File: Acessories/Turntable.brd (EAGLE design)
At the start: 80 x 50 mm, 31 parts, among them IC1 7812TV, IC2 7805TV, J1 HEADER4, M1 ARDUINO-NANO-3.0, U2 A4988, X1 MKDSN1,5/4-5,08

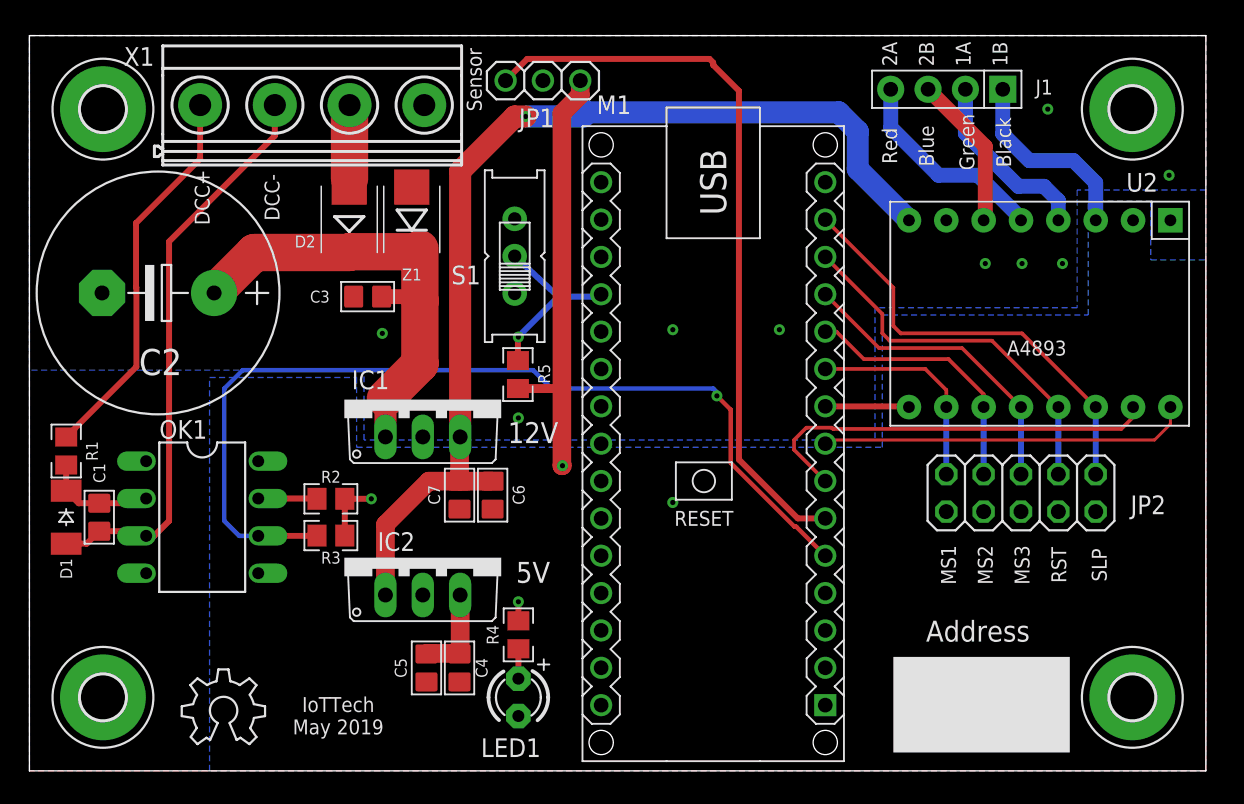
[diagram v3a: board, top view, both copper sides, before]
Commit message: Add files via upload
Updated turntable design, added 3.5mm connector for stepper motor and direct control of the stepping levels
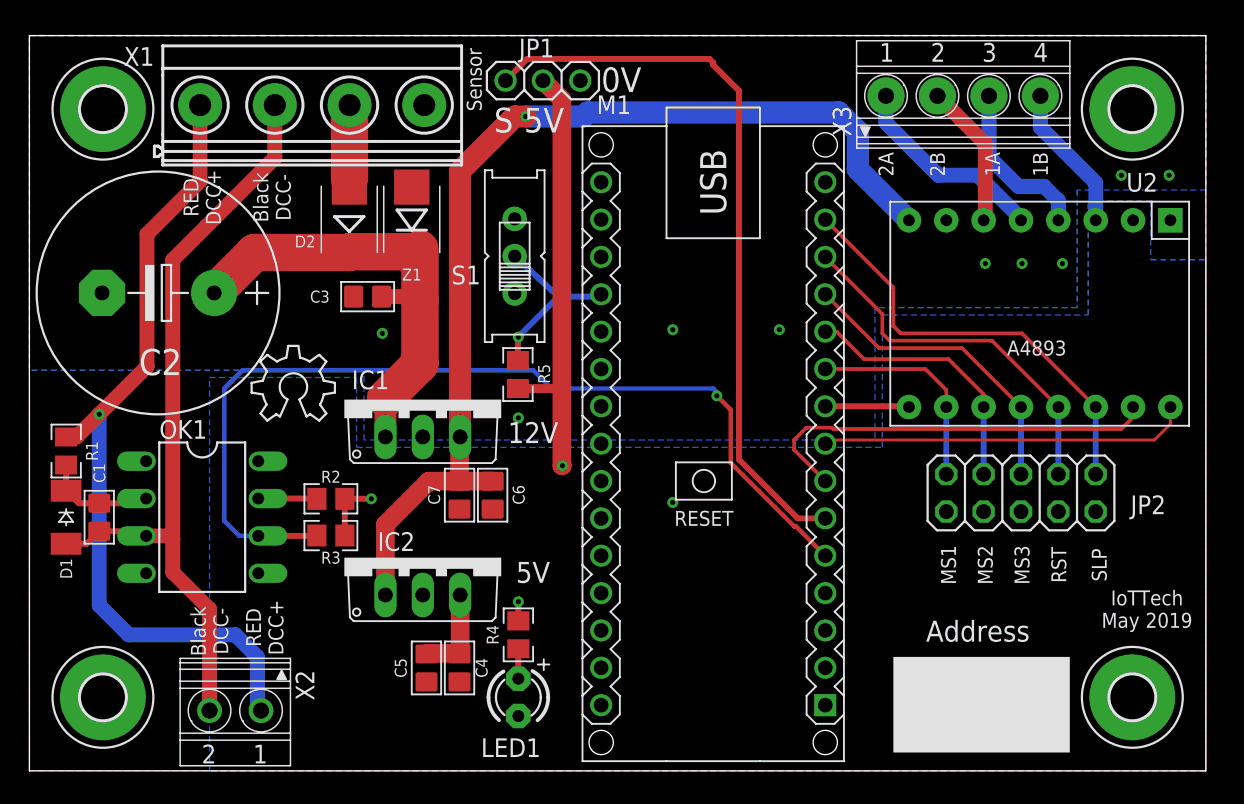
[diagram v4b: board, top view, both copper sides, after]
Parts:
- removed J1: HEADER4, GJR:HEADER4
- added X2: 1751248, con-phoenix-350:1751248
- added X3: 1751264, con-phoenix-350:1751264
- moved LOGO1 22.5 mm to (-24.9, -1.18)
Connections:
- net +5V: now also JP1.2; no longer JP1.3
- net 1A: now also X3.3; no longer J1.2
- net 1B: now also X3.4; no longer J1.1
- net 2A: now also X3.1; no longer J1.4
- net 2B: now also X3.2; no longer J1.3
- net GND: now also JP1.3; no longer JP1.2
- net TRACK1: now also X2.1
- net TRACK2: now also X2.2
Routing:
- net TRACK1: track 26.4 -> 55.7 mm, vias 0 -> 1
- net TRACK2: track 39.1 -> 52.9 mm
- net 1B: track 13.3 -> 10.0 mm
- net 1A: track 12.6 -> 11.4 mm
- net 2B: track 10.6 -> 9.85 mm
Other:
- board text added: "0V"
- board text added: "Black DCC-"
- board text added: "RED DCC+"
- board text added: "S"
- board text removed: "Black"
- board text removed: "Blue"
- board text removed: "DCC+"
- board text removed: "DCC-"
- board text removed: "Green"
- board text removed: "Red"

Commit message: Add files via upload
added 2 more sensor inputs to enable multiple sensing locations. Intended home, first engine, last engine
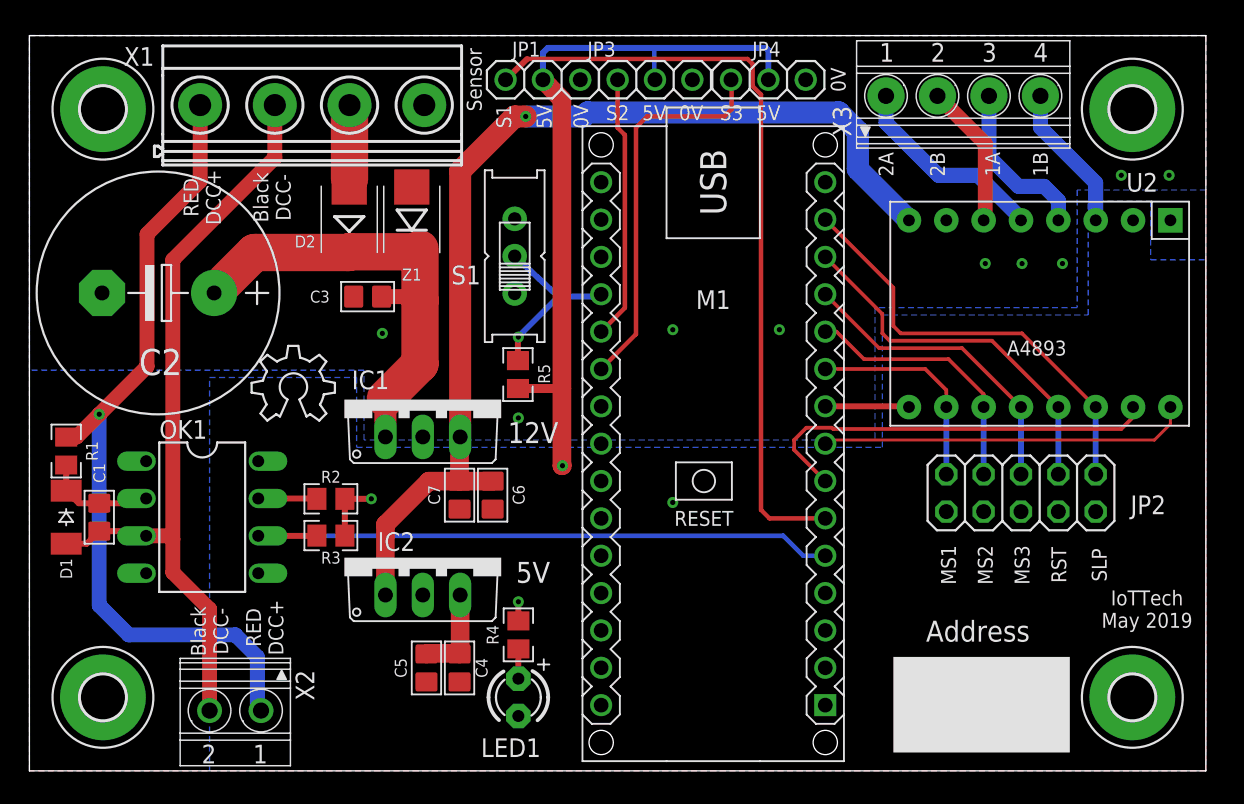
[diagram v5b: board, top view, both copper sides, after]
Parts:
- added JP3, JP4: (no value), adafruit:1X03
- moved JP1 0.06 mm to (-5.08, 22.0)
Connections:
- net POS renamed POS1
- new net POS2: JP3.1, M1.J2.11
- new net POS3: JP4.1, M1.J2.10
- net +5V: now also JP3.2, JP4.2
- net GND: now also JP3.3, JP4.3
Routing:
- net POS3: track 0.00 -> 26.4 mm
- net +5V: track 41.9 -> 63.5 mm
- net DCCIN: track 64.6 -> 43.1 mm, vias 1 -> 0
- net POS2: track 0.00 -> 18.0 mm
- net POS1: track 50.1 -> 52.7 mm
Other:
- board text added: "S1"
- board text added: "S2"
- board text added: "S3"
- board text removed: "S"
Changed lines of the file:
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@@
 <text x="36" y="-14" size="1.016" layer="21" align="center">IoTTech
 May 2019</text>
-<text x="-7.75" y="19.25" size="1.6764" layer="21" align="center">S</text>
-<text x="-5" y="19.25" size="1.6764" layer="21" align="center">5V</text>
-<text x="0.25" y="22" size="1.6764" layer="21" align="center">0V</text>
+<text x="-7.75" y="19.5" size="1.016" layer="21" rot="R90" align="center">S1</text>
+<text x="-5" y="19.5" size="1.016" layer="21" rot="R90" align="center">5V</text>
+<text x="-2.5" y="19.5" size="1.016" layer="21" rot="R90" align="center">0V</text>
 <text x="-24" y="-15.25" size="1.016" layer="21" rot="R90" align="center">RED
 DCC+</text>
 <text x="-27.75" y="-15.5" size="1.016" layer="21" rot="R90" align="center">Black
 DCC-</text>
+<text x="15" y="22" size="1.016" layer="21" rot="R90" align="center">0V</text>
+<text x="5" y="19.75" size="1.016" layer="21" rot="R180" align="center">0V</text>
+<text x="2.5" y="19.75" size="1.016" layer="21" rot="R180" align="center">5V</text>
+<text x="10.25" y="19.75" size="1.016" layer="21" rot="R180" align="center">5V</text>
+<text x="0" y="19.75" size="1.016" layer="21" rot="R180" align="center">S2</text>
+<text x="7.75" y="19.75" size="1.016" layer="21" rot="R180" align="center">S3</text>
 </plain>
 <attributes>
@@
 </element>
 <element name="M1" library="diy-modules" package="ARDUINO-NANO-3.0" value="ARDUINO-NANO-3.0" x="6.5" y="-2.75" smashed="yes" rot="R270">
-<attribute name="NAME" x="-0.25" y="19.66" size="1.27" layer="25" align="bottom-center"/>
+<attribute name="NAME" x="6.5" y="6.41" size="1.27" layer="25" align="bottom-center"/>
 <attribute name="VALUE" x="-3.66" y="-2.75" size="1.27" layer="27" rot="R270" align="top-center"/>
 </element>
@@
 <element name="H3" library="holes" package="3,0-PAD" value="MOUNT-PAD-ROUND3.0" x="-35" y="-20" smashed="yes"/>
 <element name="H4" library="holes" package="3,0-PAD" value="MOUNT-PAD-ROUND3.0" x="-35" y="20" smashed="yes"/>
-<element name="JP1" library="adafruit" library_urn="urn:adsk.eagle:library:420" package="1X03" package3d_urn="urn:adsk.eagle:package:6240710/1" value="" x="-5.08" y="21.94" smashed="yes">
-<attribute name="NAME" x="-6.7162" y="23.5188" size="1.27" layer="25" ratio="10"/>
-<attribute name="VALUE" x="-8.89" y="18.765" size="1.27" layer="27"/>
+<element name="JP1" library="adafruit" library_urn="urn:adsk.eagle:library:420" package="1X03" package3d_urn="urn:adsk.eagle:package:6240710/1" value="" x="-5.08" y="22" smashed="yes">
+<attribute name="NAME" x="-6.2162" y="24.0788" size="1.016" layer="25" ratio="10" align="center"/>
+<attribute name="VALUE" x="-8.89" y="18.825" size="1.27" layer="27"/>
 </element>
 <element name="LOGO1" library="ohw-logo" package="OSHW_6X200_NOTEXT" value="OSHW_LOGO_6MILX0200-NT" x="-24.89" y="-1.18" smashed="yes"/>
@@
 <attribute name="OC_NEWARK" value="unknown" x="-26" y="-21" size="1.778" layer="27" rot="R180" display="off"/>
 <attribute name="VALUE" x="-23.9475" y="-25.1275" size="1.27" layer="27" rot="R180"/>
+</element>
+<element name="JP3" library="adafruit" library_urn="urn:adsk.eagle:library:420" package="1X03" package3d_urn="urn:adsk.eagle:package:6240710/1" value="" x="2.54" y="22" smashed="yes">
+<attribute name="NAME" x="-1.0962" y="24.0788" size="1.016" layer="25" ratio="10" align="center"/>
+<attribute name="VALUE" x="-1.27" y="18.825" size="1.27" layer="27"/>
+</element>
+<element name="JP4" library="adafruit" library_urn="urn:adsk.eagle:library:420" package="1X03" package3d_urn="urn:adsk.eagle:package:6240710/1" value="" x="10.25" y="22" smashed="yes">
+<attribute name="NAME" x="10.1138" y="24.0788" size="1.016" layer="25" ratio="10" align="center"/>
+<attribute name="VALUE" x="6.44" y="18.825" size="1.27" layer="27"/>
 </element>
 </elements>
@@
 <contactref element="IC1" pad="2"/>
 <contactref element="IC2" pad="2"/>
+<contactref element="JP3" pad="3"/>
 <contactref element="JP1" pad="3"/>
+<contactref element="JP4" pad="3"/>
 </signal>
 <signal name="+5V">
@@
 <via x="-16.75" y="-6.5" extent="1-16" drill="0.35"/>
 <contactref element="JP1" pad="2"/>
-<wire x1="-5.08" y1="21.94" x2="-3.79" y2="20.65" width="1.27" layer="1"/>
+<wire x1="-5.08" y1="22" x2="-3.79" y2="20.65" width="1.27" layer="1"/>
 <wire x1="-3.79" y1="20.65" x2="-3.79" y2="1" width="1.27" layer="1"/>
+<contactref element="JP3" pad="2"/>
+<contactref element="JP4" pad="2"/>
+<wire x1="-5.08" y1="22" x2="-5.08" y2="23.8318" width="0.4064" layer="16"/>
+<wire x1="-5.08" y1="23.8318" x2="-4.75" y2="24.1618" width="0.4064" layer="16"/>
+<wire x1="-4.75" y1="24.1618" x2="2.5" y2="24.1618" width="0.4064" layer="16"/>
+<wire x1="2.5" y1="24.1618" x2="10.0882" y2="24.1618" width="0.4064" layer="16"/>
+<wire x1="10.0882" y1="24.1618" x2="10.25" y2="24" width="0.4064" layer="16"/>
+<wire x1="10.25" y1="24" x2="10.25" y2="22" width="0.4064" layer="16"/>
+<wire x1="2.5" y1="24.1618" x2="2.5" y2="22.04" width="0.3048" layer="16"/>
+<wire x1="2.5" y1="22.04" x2="2.54" y2="22" width="0.3048" layer="16"/>
 </signal>
 <signal name="DCCIN">
@@
 <contactref element="OK1" pad="6"/>
 <contactref element="M1" pad="J1.5"/>
-<wire x1="-24.44" y1="-9.02" x2="-25.73" y2="-9.02" width="0.3048" layer="16"/>
-<wire x1="-25.73" y1="-9.02" x2="-26.75" y2="-8" width="0.3048" layer="16"/>
-<wire x1="-26.75" y1="-8" x2="-26.75" y2="1" width="0.3048" layer="16"/>
-<wire x1="-26.75" y1="1" x2="-25.5" y2="2.25" width="0.3048" layer="16"/>
-<wire x1="-25.5" y1="2.25" x2="-5.75" y2="2.25" width="0.3048" layer="16"/>
-<wire x1="-5.75" y1="2.25" x2="-4.5" y2="1" width="0.3048" layer="16"/>
-<wire x1="6.5" y1="1" x2="6.75" y2="0.75" width="0.3048" layer="16"/>
-<wire x1="6.75" y1="0.75" x2="6.75" y2="0.5" width="0.3048" layer="16"/>
-<via x="6.75" y="0.5" extent="1-16" drill="0.35"/>
-<wire x1="6.75" y1="0.5" x2="7.6912" y2="-0.4412" width="0.3048" layer="1"/>
-<wire x1="7.6912" y1="-0.4412" x2="7.6912" y2="-4.06146875" width="0.3048" layer="1"/>
-<wire x1="7.6912" y1="-4.06146875" x2="12.01853125" y2="-8.3888" width="0.3048" layer="1"/>
-<wire x1="12.01853125" y1="-8.3888" x2="12.1388" y2="-8.3888" width="0.3048" layer="1"/>
-<wire x1="12.1388" y1="-8.3888" x2="14.12" y2="-10.37" width="0.3048" layer="1"/>
-<wire x1="-4.5" y1="1" x2="6.5" y2="1" width="0.3048" layer="16"/>
+<wire x1="11.25" y1="-9" x2="12.62" y2="-10.37" width="0.3048" layer="16"/>
 <wire x1="-24.44" y1="-9.02" x2="-20.47" y2="-9.02" width="0.4064" layer="1"/>
 <wire x1="-20.47" y1="-9.02" x2="-20.45" y2="-9" width="0.4064" layer="1"/>
+<wire x1="14.12" y1="-10.37" x2="12.62" y2="-10.37" width="0.3048" layer="16"/>
+<wire x1="-24.44" y1="-9.02" x2="11.23" y2="-9.02" width="0.3048" layer="16"/>
+<wire x1="11.23" y1="-9.02" x2="11.25" y2="-9" width="0.3048" layer="16"/>
 </signal>
 <signal name="N$2">
@@
 <wire x1="19.76" y1="-0.21" x2="19.81" y2="-0.26" width="0.4064" layer="1"/>
 </signal>
-<signal name="POS">
+<signal name="POS1">
+<contactref element="JP1" pad="1"/>
+<wire x1="-7.62" y1="22" x2="-6.1482" y2="23.4118" width="0.4064" layer="1"/>
 <contactref element="M1" pad="J1.6"/>
-<contactref element="JP1" pad="1"/>
-<wire x1="14.12" y1="-7.83" x2="12.25" y2="-7.83" width="0.4064" layer="1"/>
-<wire x1="12.25" y1="-7.83" x2="8.25" y2="-3.83" width="0.4064" layer="1"/>
-<wire x1="6.5" y1="23" x2="8.25" y2="21.25" width="0.4064" layer="1"/>
-<wire x1="8.25" y1="-3.83" x2="8.25" y2="21.25" width="0.4064" layer="1"/>
-<wire x1="-7.62" y1="21.94" x2="-6.1482" y2="23.4118" width="0.4064" layer="1"/>
-<wire x1="-6.1482" y1="23.4118" x2="6.25" y2="23.4118" width="0.4064" layer="1"/>
-<wire x1="6.25" y1="23.4118" x2="6.5" y2="23.1618" width="0.4064" layer="1"/>
-<wire x1="6.5" y1="23.1618" x2="6.5" y2="23" width="0.4064" layer="1"/>
+<wire x1="-6.1482" y1="23.4118" x2="8.8382" y2="23.4118" width="0.3048" layer="1"/>
+<wire x1="9.75" y1="20.9913125" x2="9.75" y2="-7.25" width="0.3048" layer="1"/>
+<wire x1="9.1832" y1="23.0668" x2="9.1832" y2="21.5581125" width="0.3048" layer="1"/>
+<wire x1="9.1832" y1="21.5581125" x2="9.75" y2="20.9913125" width="0.3048" layer="1"/>
+<wire x1="9.75" y1="-7.25" x2="10.33" y2="-7.83" width="0.3048" layer="1"/>
+<wire x1="10.33" y1="-7.83" x2="14.12" y2="-7.83" width="0.3048" layer="1"/>
+<wire x1="8.8382" y1="23.4118" x2="9.1832" y2="23.0668" width="0.3048" layer="1"/>
 </signal>
 <signal name="STEP">
@@
 <wire x1="19.25" y1="4.75" x2="27.5" y2="4.75" width="0.254" layer="1"/>
 </signal>
+<signal name="POS2">
+<contactref element="JP3" pad="1"/>
+<contactref element="M1" pad="J2.11"/>
+<wire x1="0.4929" y1="18.2380875" x2="0" y2="18.7309875" width="0.3048" layer="1"/>
+<wire x1="0" y1="18.7309875" x2="0" y2="22" width="0.3048" layer="1"/>
+<wire x1="-1.12" y1="4.87" x2="0.4929" y2="6.4829" width="0.3048" layer="1"/>
+<wire x1="0.4929" y1="6.4829" x2="0.4929" y2="18.2380875" width="0.3048" layer="1"/>
+</signal>
+<signal name="POS3">
+<contactref element="JP4" pad="1"/>
+<contactref element="M1" pad="J2.10"/>
+<wire x1="-1.12" y1="2.33" x2="1.25" y2="4.7" width="0.3048" layer="1"/>
+<wire x1="1.25" y1="18.75" x2="2" y2="19.5" width="0.3048" layer="1"/>
+<wire x1="7.25" y1="19.5" x2="7.75" y2="20" width="0.3048" layer="1"/>
+<wire x1="7.75" y1="20" x2="7.75" y2="21.96" width="0.3048" layer="1"/>
+<wire x1="7.75" y1="21.96" x2="7.71" y2="22" width="0.3048" layer="1"/>
+<wire x1="1.25" y1="4.7" x2="1.25" y2="18.75" width="0.3048" layer="1"/>
+<wire x1="2" y1="19.5" x2="7.25" y2="19.5" width="0.3048" layer="1"/>
+</signal>
 </signals>
